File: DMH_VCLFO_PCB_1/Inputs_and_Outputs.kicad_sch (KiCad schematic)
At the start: 7 parts, among them J1 TS_Jack_6.35mm_Sw, J2 TS_Jack_6.35mm_Sw, J200 IDC_02x05, J3 TS_Jack_6.35mm_Sw, J5 TS_Jack_6.35mm_Sw, J50 Conn_01x06, J60 Conn_01x06

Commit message: schematic design in progress
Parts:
- removed J1, J2, J3, J5: TS_Jack_6.35mm_Sw, SynthStuff:CUI_MJ-63052A, symbol SynthStuff:TS_Jack_6.35mm_Sw
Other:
- moved on the sheet: J200

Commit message: Ready for breadboarding
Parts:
- removed J200: IDC_02x05, SynthStuff:IDC-Header_2x05_P2.54mm_Vertical_BackBone, symbol SynthStuff:BackBone_Connector_10Pin
- removed J50, J60: Conn_01x06, Connector_PinSocket_2.54mm:PinSocket_1x06_P2.54mm_Vertical, symbol Connector_Generic:Conn_01x06
- added J1, J2, J3, J4, J5, J6: TS_Jack_6.35mm_Sw, SynthStuff:CUI_MJ-63052A, symbol SynthStuff:TS_Jack_6.35mm_Sw
- added J10: IDC_02x05, SynthStuff:IDC-Header_2x05_P2.54mm_Vertical_BackBone, symbol SynthStuff:BackBone_Connector_10Pin
- added R10, R11, R12, R13, R14, R15, R16, R17, R18, R19, R20, R21, R22, R23, R24, R25, R26, R27, R28, R5, R6, R7, R8, R9: 100k, Resistor_THT:R_Axial_DIN0207_L6.3mm_D2.5mm_P7.62mm_Horizontal, symbol Device:R_US
- added R29, R30, R31, R32, R33, R34: 1k, Resistor_THT:R_Axial_DIN0207_L6.3mm_D2.5mm_P7.62mm_Horizontal, symbol Device:R_US
- added R3: 270R, Resistor_THT:R_Axial_DIN0207_L6.3mm_D2.5mm_P7.62mm_Horizontal, symbol Device:R_US
- added R4: 33k, Resistor_THT:R_Axial_DIN0207_L6.3mm_D2.5mm_P7.62mm_Horizontal, symbol Device:R_US
- added RV1, RV2: B100k, SynthStuff:Potentiometer_TT_P110KH1, symbol Device:R_Potentiometer_US
- added RV3: 50k, Potentiometer_THT:Potentiometer_Bourns_3296X_Horizontal, symbol Device:R_Potentiometer_Trim_US
- added SW1, SW3, SW4: SW_SPDT, SynthStuff:Toggle_Switch_TE, symbol Switch:SW_SPDT
- added SW2: SPDT_OnOffOn, SynthStuff:Toggle_Switch_TE, symbol SynthStuff:SW_SPDT_OnOffOn
- added U1, U2: TL074, Package_DIP:DIP-14_W7.62mm_Socket, symbol Amplifier_Operational:TL074
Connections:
- new net: R24.2, R30.1, U1.8
- new net: J4.T, R30.2
- new net: R26.2, R32.1, U2.1
- new net: R16.1, R26.1, U2.2 (-)
- new net: R14.2, R15.2, U2.3 (+)
- new net: J5.T, SW3.2 (B)
- new net: R34.1, SW3.3 (C)
- new net: R22.1, R28.1, U2.9 (-)
- new net: R4.2, RV3.1, U1.2 (-)
- new net: R11.1, R14.1, R17.1, R20.1, R5.1, R8.1, SW2.2 (B)
- new net: R5.2, R6.2, U1.5 (+)
- new net: R25.2, R31.1, U1.14
- new net: R20.2, R21.2, U2.10 (+)
- new net: J1.T, R4.1, RV2.3
- new net: R8.2, R9.2, U1.10 (+)
- new net: R3.1, RV1.1
- new net: R19.1, R27.1, U2.6 (-)
- new net: R11.2, R12.2, U1.12 (+)
- new net: R13.1, R25.1, U1.13 (-)
- new net: R28.2, R34.2, U2.8
- new net: R17.2, R18.2, U2.5 (+)
- new net: RV2.2, U1.3 (+)
- new net: R27.2, R33.1, U2.7
- new net: R33.2, SW4.1 (A)
- new net: R23.2, R29.1, U1.7
- new net: R10.1, R24.1, U1.9 (-)
- new net: J6.T, SW4.2 (B)
- new net: R23.1, R7.1, U1.6 (-)
- new net: J3.T, R32.2
- new net: U2.13 (-), U2.14
- new net +12V: RV1.3
- new net +5V: SW2.3 (C)
- new net -5V: SW2.1 (A)
- new net CV A: RV3.2, RV3.3, U1.1
- new net CV In A TN: J1.TN, J10.1 (Pin_1)
- new net GND: J1.S, J10.10 (Pin_10), J10.4 (Pin_4), J10.5 (Pin_5), J10.9 (Pin_9), J2.S, J3.S, J4.S, J5.S, J6.S, R10.2, R13.2, R16.2, R19.2, R22.2, R3.2, R7.2, RV2.1, U2.12 (+)
- new net Out A Rmp/Rnd TN: J10.6 (Pin_6), J5.TN
- new net Out A Saw TN: J10.3 (Pin_3), J4.TN
- new net Out A Sin/Tri TN: J10.7 (Pin_7), J6.TN
- new net Out A Sqr TN: J10.8 (Pin_8), J3.TN
- new net Pot A: RV1.2
- new net Rmp: R12.1
- new net Rmp_Out: R31.2, SW3.1 (A)
- new net Rnd: R21.1
- new net Rng_Sw_1: SW1.1 (A)
- new net Rng_Sw_2: SW1.2 (B)
- new net Saw: R9.1
- new net Sin: R18.1
- new net Sqr: R15.1
- new net Sync A: J2.T
- new net Sync A TN: J10.2 (Pin_2), J2.TN
- new net Tri: R6.1
- new net Tri_Out: R29.2, SW4.3 (C)
- no-connect marks 0 -> 1

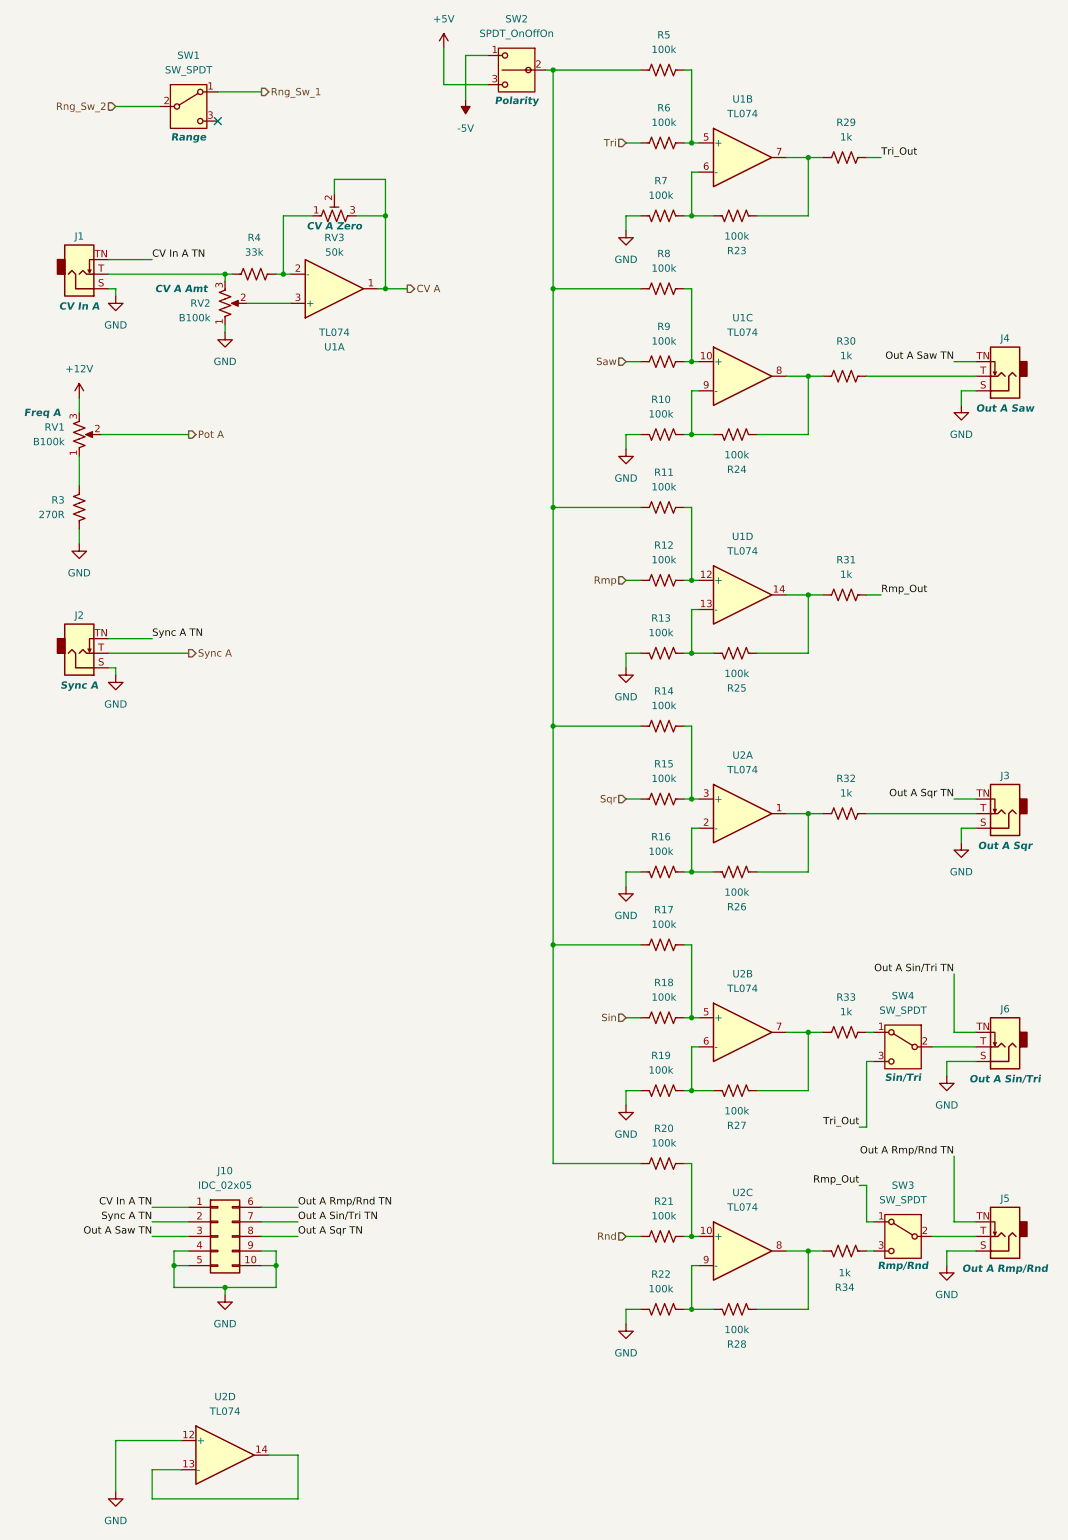
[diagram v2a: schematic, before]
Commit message: Fixed issue with polarity selector
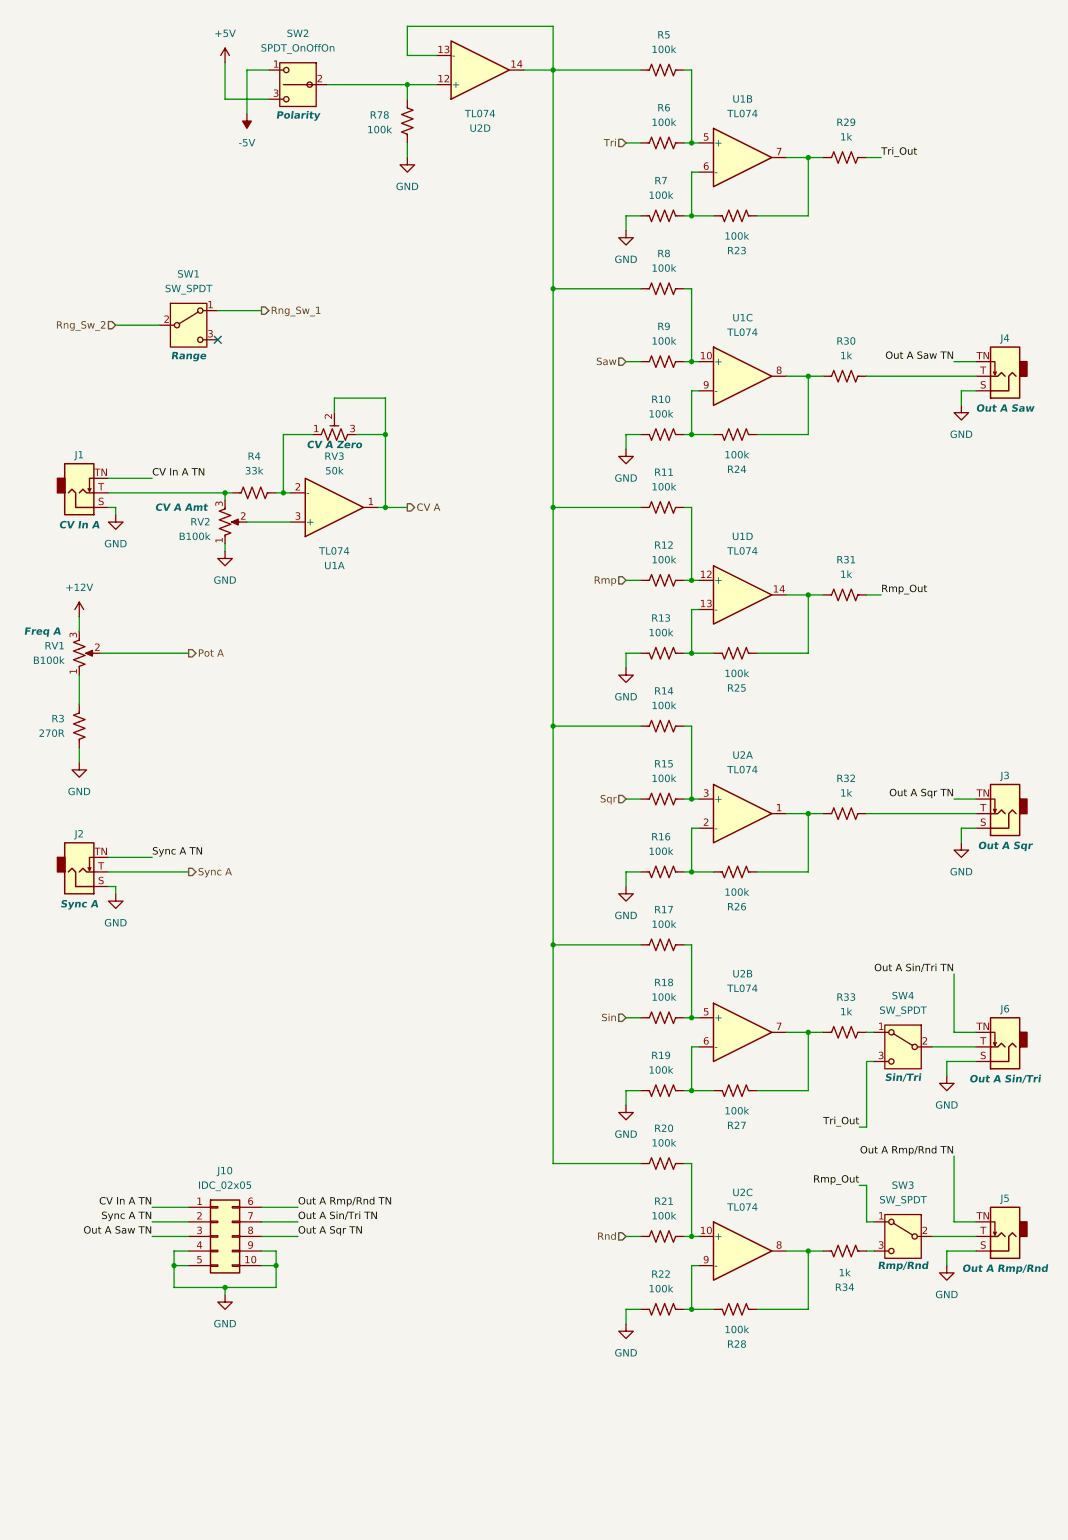
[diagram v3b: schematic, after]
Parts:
- added R78: 100k, Resistor_THT:R_Axial_DIN0207_L6.3mm_D2.5mm_P7.62mm_Horizontal, symbol Device:R_US
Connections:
- net GND: now also R78.1; no longer U2.12 (+)
- net at R11.1, R14.1, R17.1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: now also U2.13 (-), U2.14; no longer SW2.2 (B)
- new net: R78.2, SW2.2 (B), U2.12 (+)
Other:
- moved on the sheet: J1, J2, R3, R4, RV1, RV2, RV3, SW1, SW2, U1A
